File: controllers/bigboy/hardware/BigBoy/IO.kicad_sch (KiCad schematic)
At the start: 43 parts, among them J2 Amphenol 10118194-0001LF, J5 SPI2, J6 USART1, J7 Hirose DM3D-S, J7 I^{2}C1, J8 USART2, J9 Bel SI-60062-F, U4 LAN8742A

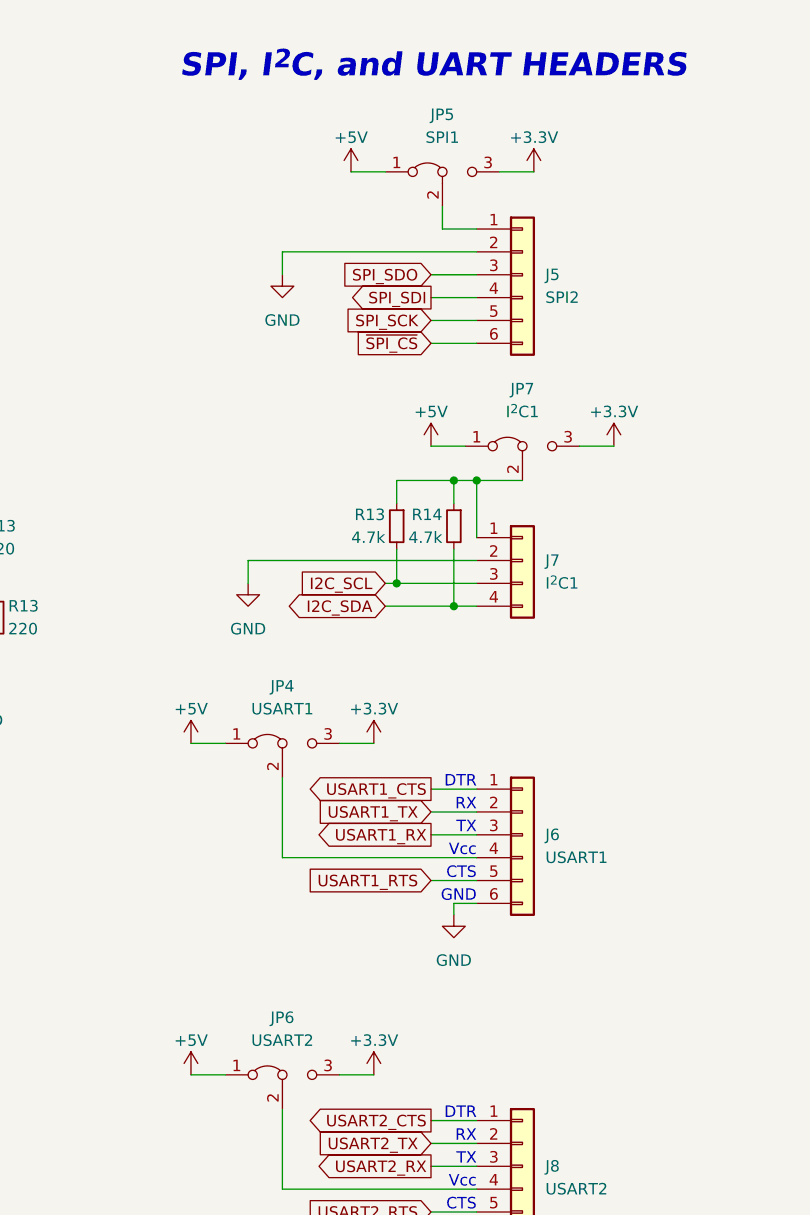
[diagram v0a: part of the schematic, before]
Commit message: Reorganized to make it easier to group hardware and firmware files together
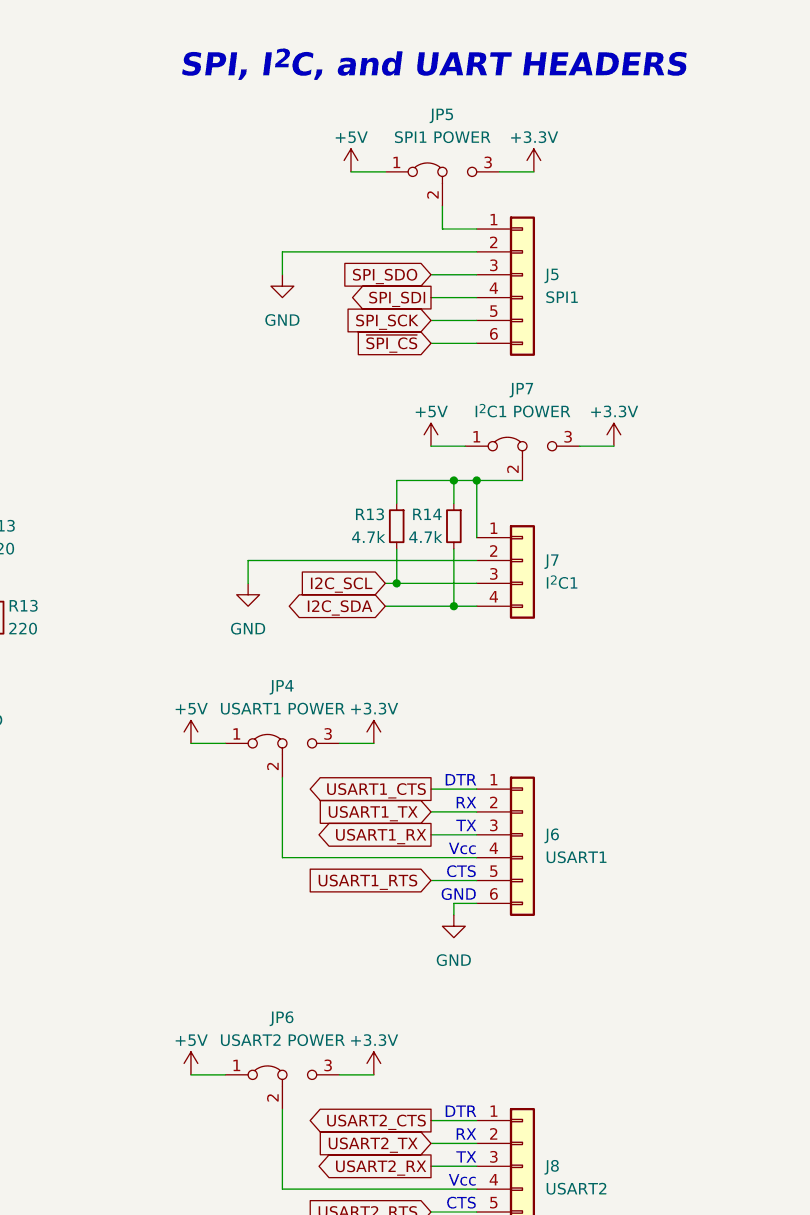
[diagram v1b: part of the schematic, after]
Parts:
- J5: value SPI2 -> SPI1
- JP4: value USART1 -> USART1 POWER
- JP5: value SPI1 -> SPI1 POWER
- JP6: value USART2 -> USART2 POWER
- JP7: value I^{2}C1 -> I^{2}C1 POWER
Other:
- title: IVC-k30 -> BigBoy

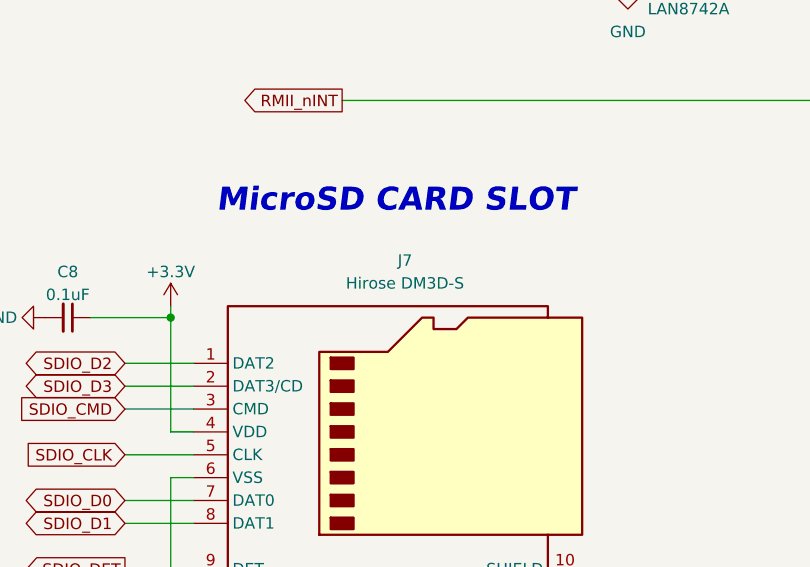
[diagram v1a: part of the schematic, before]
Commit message: Most of the routing for BigBoy is done
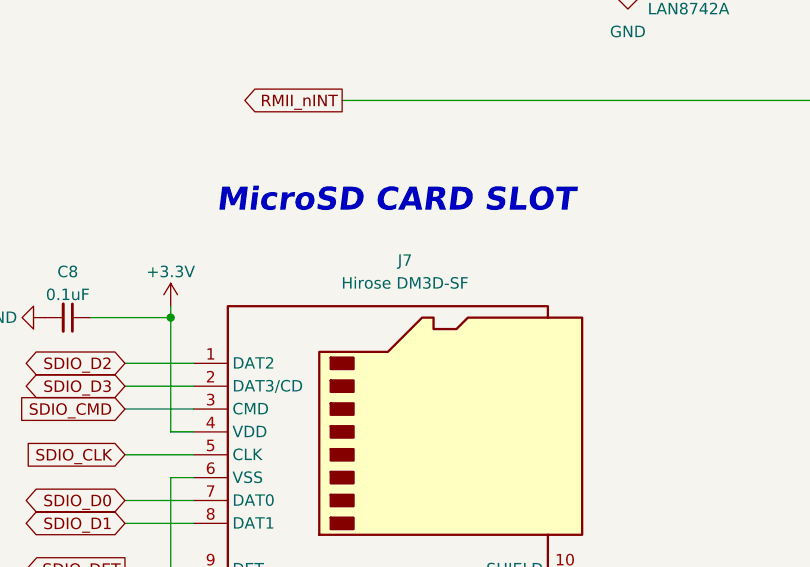
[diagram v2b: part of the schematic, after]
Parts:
- J7: value Hirose DM3D-S -> Hirose DM3D-SF
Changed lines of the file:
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@@
       (effects (font (size 1.27 1.27)))
     )
-    (property "Value" "Hirose DM3D-S" (at 60.325 144.78 0)
+    (property "Value" "Hirose DM3D-SF" (at 60.325 144.78 0)
       (effects (font (size 1.27 1.27)))
     )

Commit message: BigBoy Rev.1 is complete and ready to order
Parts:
- removed JP7: I^{2}C1 POWER, Connector_PinHeader_2.54mm:PinHeader_1x03_P2.54mm_Vertical, symbol Jumper:Jumper_3_Bridged12
- added J14: STEMMA, Connector_JST:JST_SH_SM04B-SRSS-TB_1x04-1MP_P1.00mm_Horizontal, symbol Connector:Conn_01x04_Socket
- added JP6: SH, Jumper:SolderJumper-2_P1.3mm_Open_RoundedPad1.0x1.5mm, symbol Jumper:SolderJumper_2_Open
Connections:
- net +3.3V: now also J7.2 (Pin_2), R13.1, R14.1, J14.2 (Pin_2)
- net GND: now also J7.1 (Pin_1), J14.1 (Pin_1), JP6.2 (B); no longer J7.2 (Pin_2), J9.8, J9.SH
- net I2C_SCL: now also J7.4 (Pin_4), J14.4 (Pin_4); no longer J7.3 (Pin_3)
- net I2C_SDA: now also J7.3 (Pin_3), J14.3 (Pin_3); no longer J7.4 (Pin_4)
- new net: J9.8, J9.SH, JP6.1 (A)
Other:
- moved on the sheet: J6, J8, JP4, JP6, R13, R14
